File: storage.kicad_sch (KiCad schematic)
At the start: 14 parts, among them J11 microSD, Molex 104031-0811 pu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, U24 W25Q128JVSIQ, 128 Mbit QSPI N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

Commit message: Replace BMI088 with ICM-45686; vendor all footprints and 3D models for layout
Sensors: U21 is now the TDK ICM-45686 (single AP_CS on GPIO20 as IMU_CS,
INT1/INT2 on GPIO23/24, GPIO21 spare, R49 dropped, VDD+VDDIO on V3V3_ANA
with 100 nF + 1 uF each). Project-local symbol, footprint and stand-in STEP;
footprint numbering verified against DS-000577 Rev 1.0 Sec 11.2 (CCW, top
view). BMI088_SPI derived-symbol machinery removed from the generator.

Layout readiness: new tools/audit_footprints.py checks every component for
a resolvable footprint and present 3D model (128/128 OK). The seven official
KiCad footprints whose STEP files are absent from kicad-packages3d 10.0.6
are vendored into MARV_Packages.pretty with project-local models in
MARV_Packages.3dshapes: manufacturer STEPs (Coilcraft XGL4030, Molex
104031-0811), EasyEDA model (HRO TYPE-C-31-M-12), FreeCAD-generated bodies
from tools/3d/ (RP2354B QFN-80, TPS62913 RPU0010A, TPS2121 RUX0012A, Amass
XT30PW-M), and KiCad generic stand-ins (BMP581, ADXL375). Model offsets were
derived by measurement and confirmed in a rendered check board.
PROVENANCE.md records source, licence and SHA256 per model; LIBRARIES.md
lists the pre-fab 3D-viewer checks and the unverified dimensions.

Checks: build idempotent, ERC 0/0, check_power_netlist 149 mappings /
128 components, run_power_checks PASS, audit 0 needing action.

Co-Authored-By: Claude Fable 5.1 <noreply@anthropic.com>
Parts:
- J11: footprint Connector_Card:microSD_HC_Molex_104031-0811 -> MARV_Packages:microSD_HC_Molex_104031-0811

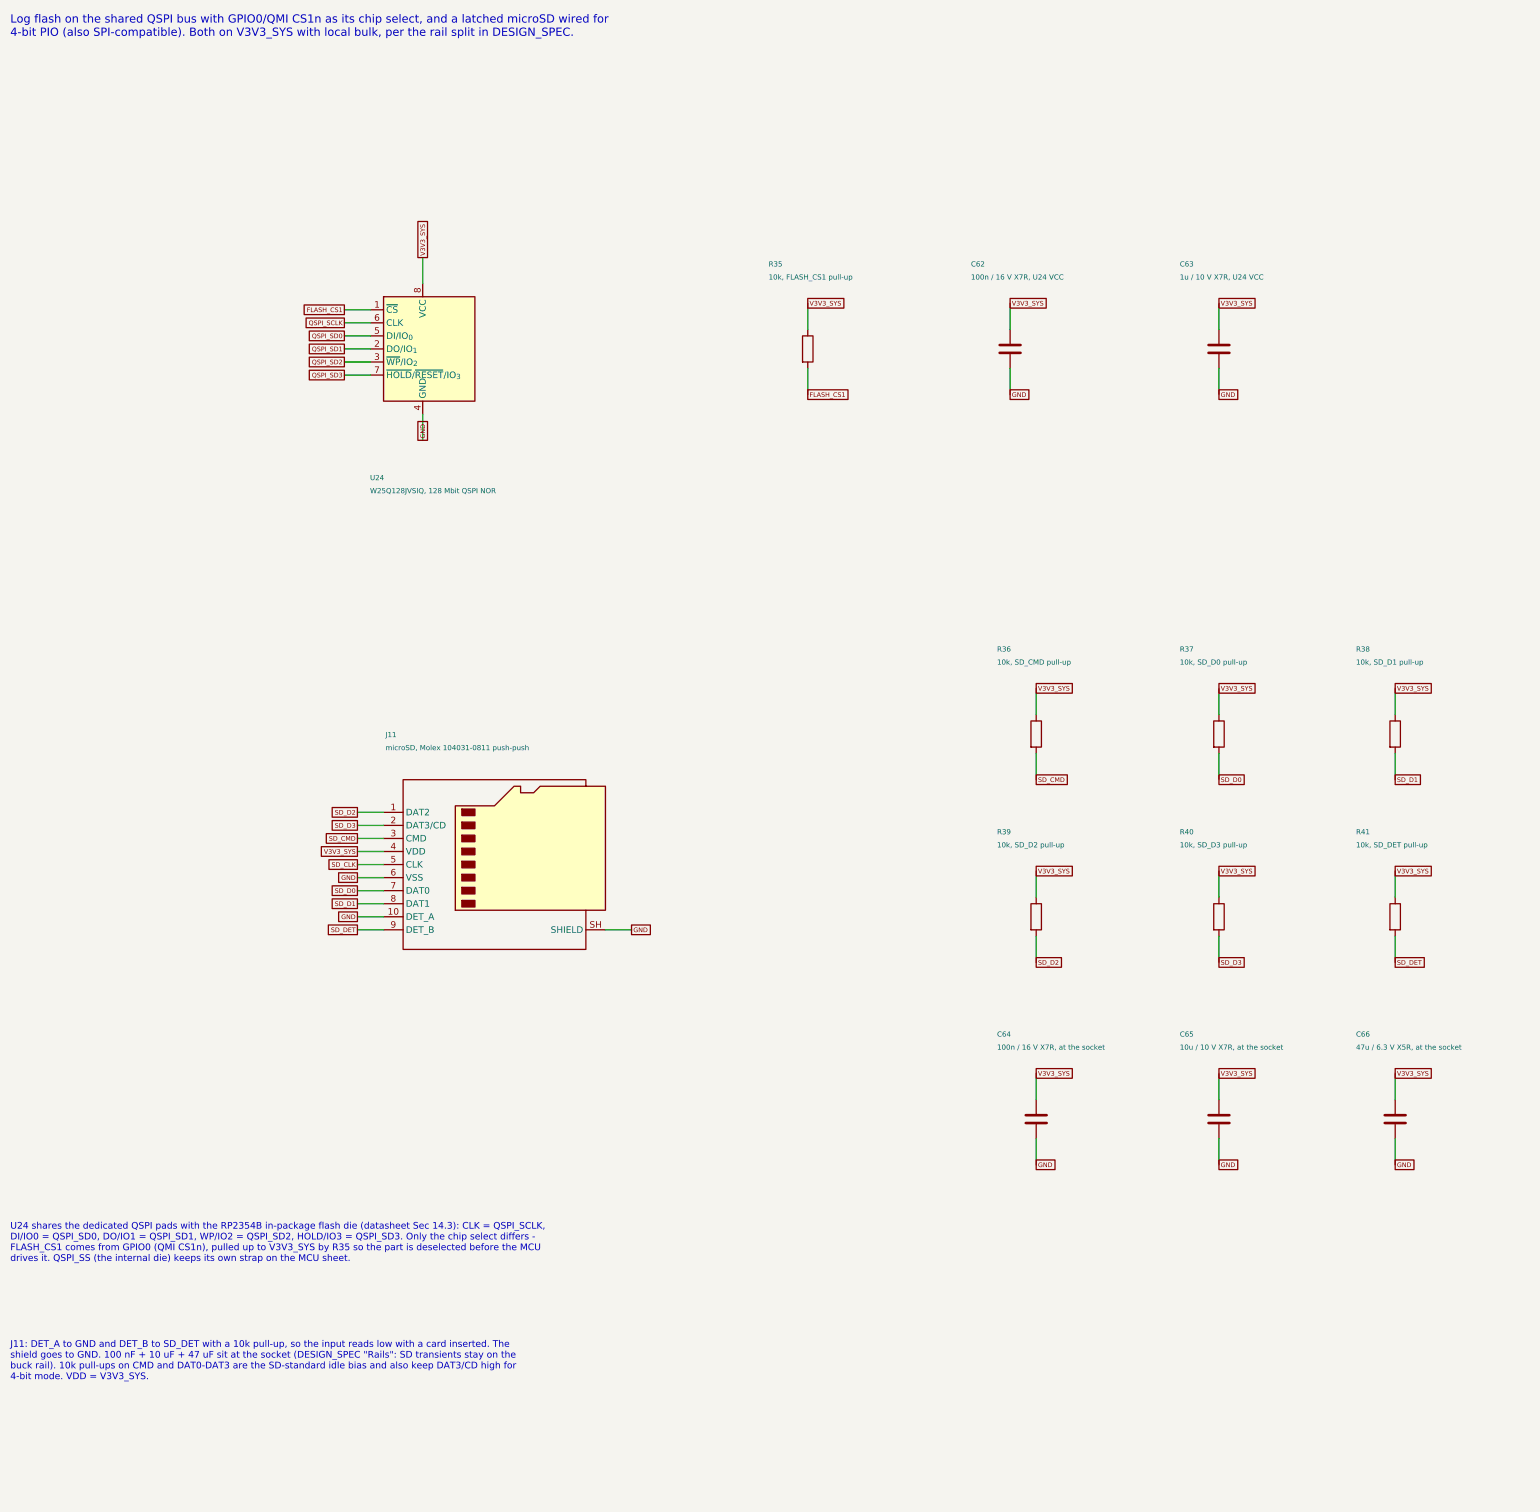
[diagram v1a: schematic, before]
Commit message: Physical design: VBAT-in buck, ESC pad row, pad-row IO, 50 mm single-sided board
Power: the FC now takes raw 2-6S VBAT from the MicoAir AM32 4-in-1 ESC pad
row (CURR TX M4 M3 M2 M1 VBAT GND, J3) through an AP63205WU 5 V/2 A buck
(U26, XGL4030-472, 3 x 22 uF) into the existing TPS2121 mux; XT30 and its
TVS removed. VBAT sense 100k/10k (36 V FS) on ADC0, ESC current sense on
ADC2, ESC KISS telemetry on GPIO30.

IO per the physical spec (DESIGN_SPEC "Physical design"): solder pad rows
for GPS/ELRS/MAG (JST-GH removed), DBG and buzzer; 3x4 servo block for
PWM5-8; 2x6 spare-IO block; WS2812C-2020 RGB LED replaces the two discrete
LEDs; buzzer moved off-board to pads; flash socket is the 150-mil SOIC-8
(W25Q64 default, APS6404L PSRAM alternative); four 4.0 mm grommet holes on
the 30.5 mm pattern. Passives moved to 0402/0603 for the single-sided
envelope.

Board: tools/setup_pcb.py regenerates MARV-V2.kicad_pcb from the netlist —
50 x 50 mm, 4-layer JLC 7628 stack-up, net classes incl. a 90 ohm USB pair,
edge-anchored connectors, coarse interior placement, silk pad labels.
DRC leaves only unrouted items. The BMP581 project footprint had its 2-pad
edges at +/-0.5 mm (corner pads overlapped, three nets shorted); corrected
to Bosch Fig. 32 (+/-0.25 mm, 0.20 mm gaps).

Checks: ERC 0/0, 217 pin mappings / 139 components, run_power_checks PASS,
audit 139/139, pcb DRC unrouted-only.

Co-Authored-By: Claude Fable 5.1 <noreply@anthropic.com>
Claude-Session: https://claude.ai/code/session_01U6Ud7JA3CDTJZVcZZr5sx1
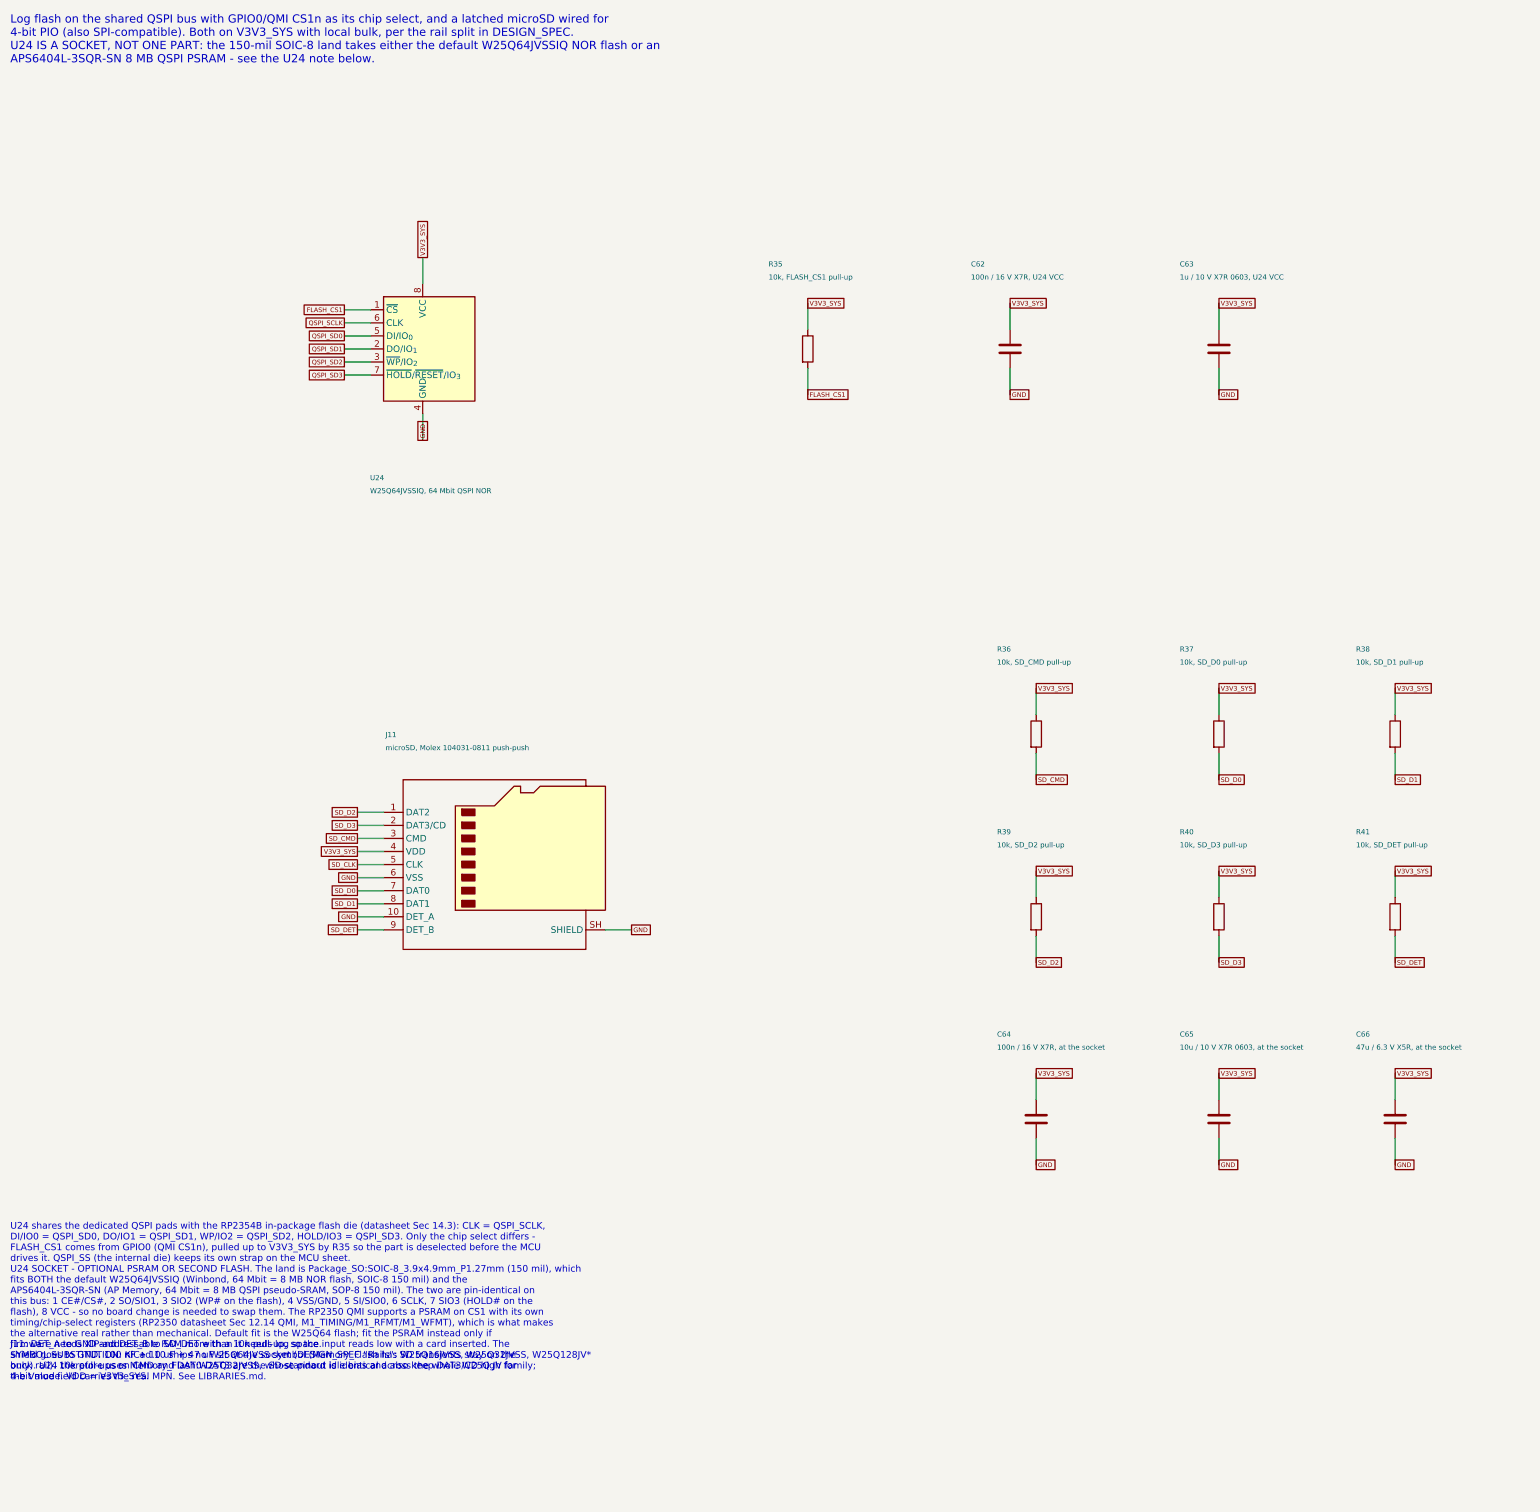
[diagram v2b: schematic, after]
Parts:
- C62, C64: footprint Capacitor_SMD:C_0805_2012Metric -> Capacitor_SMD:C_0402_1005Metric
- C63: value 1u / 10 V X7R, U24 VCC -> 1u / 10 V X7R 0603, U24 VCC; footprint Capacitor_SMD:C_0805_2012Metric -> Capacitor_SMD:C_0603_1608Metric
- C65: value 10u / 10 V X7R, at the socket -> 10u / 10 V X7R 0603, at the socket; footprint Capacitor_SMD:C_1206_3216Metric -> Capacitor_SMD:C_0603_1608Metric
- R35, R36, R37, R38, R39, R40, R41: footprint Resistor_SMD:R_0603_1608Metric -> Resistor_SMD:R_0402_1005Metric
- U24: value W25Q128JVSIQ, 128 Mbit QSPI NOR -> W25Q64JVSSIQ, 64 Mbit QSPI NOR; footprint Package_SO:SOIC-8_5.3x5.3mm_P1.27mm -> Package_SO:SOIC-8_3.9x4.9mm_P1.27mm; symbol Memory_Flash:W25Q128JVS -> Memory_Flash:W25Q32JVSS
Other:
- note added: "Log flash on the shared QSPI bus with GPIO0/QMI CS1n as its chip select, and a latched microSD wired for 4-bit PIO (also SPI-compatible). Both on V3V3_SYS with local bulk, per the rail split in DESIGN_SPEC. U24 IS A SOCKET, NOT ONE PART: the 150-mil SOIC-8 land takes either the default W25Q64JVSSIQ NOR flash or an APS6404L-3SQR-SN 8 MB QSPI PSRAM - see the U24 note below."
- note removed: "Log flash on the shared QSPI bus with GPIO0/QMI CS1n as its chip select, and a latched microSD wired for 4-bit PIO (also SPI-compatible). Both on V3V3_SYS with local bulk, per the rail split in DESIGN_SPEC."

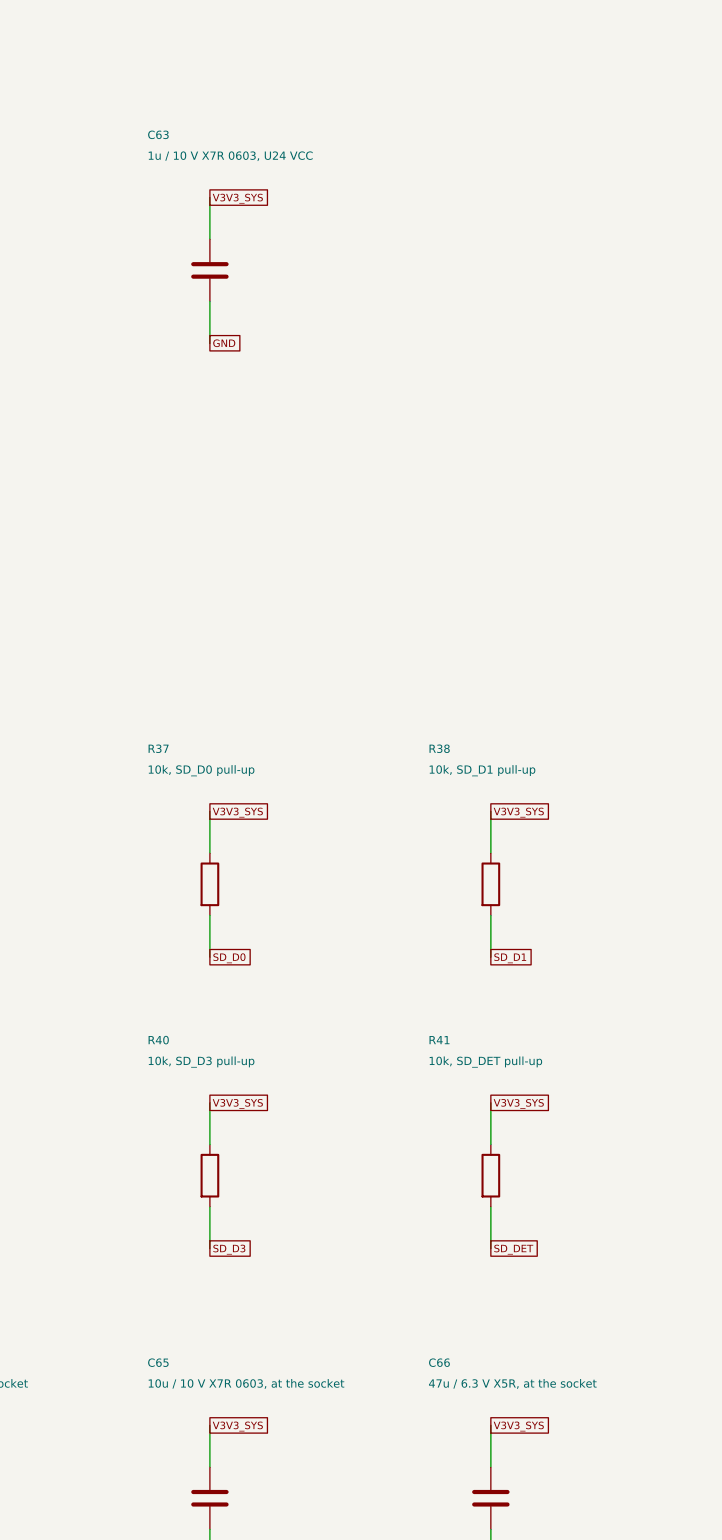
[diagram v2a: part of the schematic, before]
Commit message: Remove buzzer; passives to 0201/0402; GPIO28 to spare-IO block
Buzzer pads J15, driver Q20/D22/R33/R34 and the BUZZ nets removed; GPIO28
now terminates on J16 pin 12 (was a second GND). Resistors 0201, caps
<= 4.7 uF 0402, 22 uF/10 V 0603, 22 uF/25 V and 10 uF/50 V 0805, 47 uF
0805; USB net-class clearance 0.18 mm so the 0201 series resistors on the
pair pass DRC. Board regenerated at 50 x 50 mm (courtyard fill 63.5 %);
DRC unrouted-only. 134 components, 105 nets; ERC 0/0, 213 pin mappings,
run_power_checks PASS, audit 134/134.

Co-Authored-By: Claude Fable 5.1 <noreply@anthropic.com>
Claude-Session: https://claude.ai/code/session_01U6Ud7JA3CDTJZVcZZr5sx1
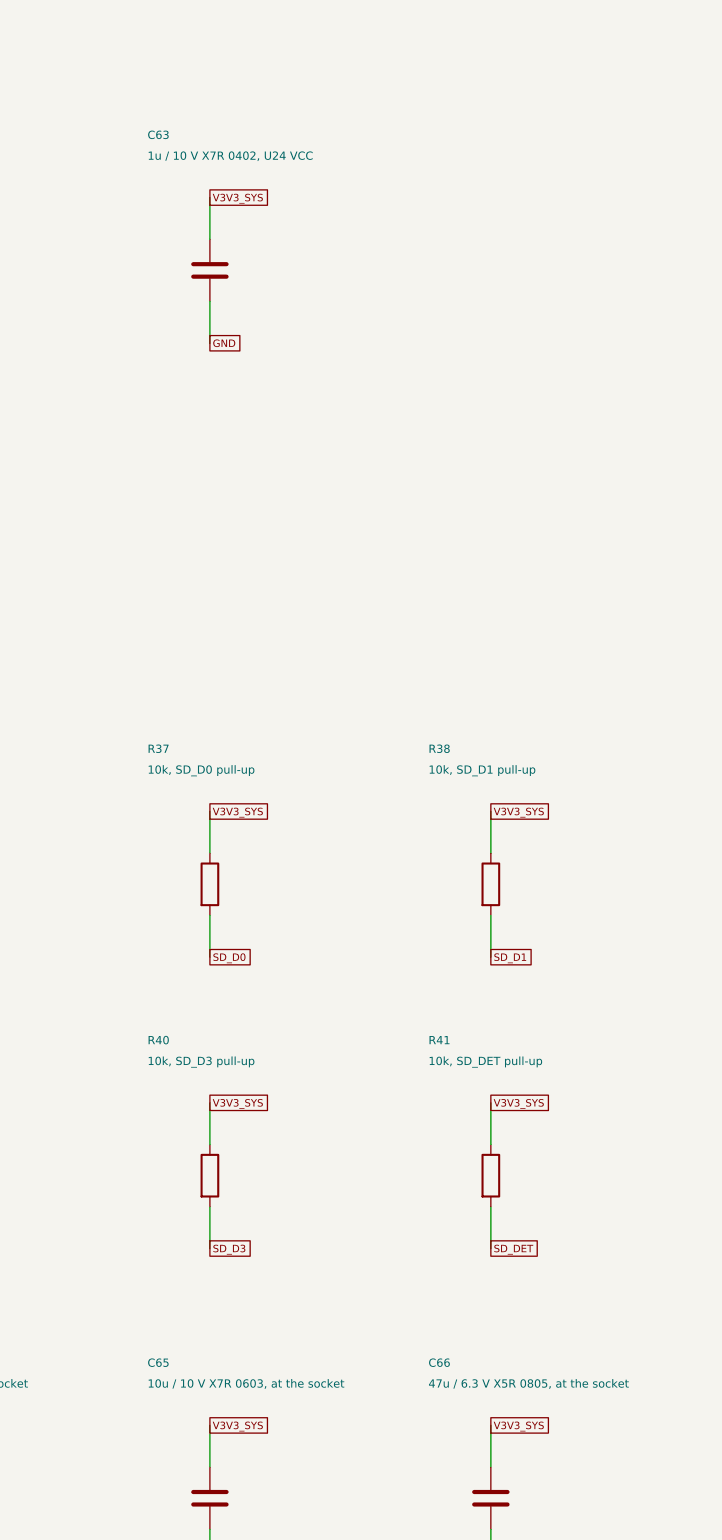
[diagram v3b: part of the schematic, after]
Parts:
- C63: value 1u / 10 V X7R 0603, U24 VCC -> 1u / 10 V X7R 0402, U24 VCC; footprint Capacitor_SMD:C_0603_1608Metric -> Capacitor_SMD:C_0402_1005Metric
- C66: value 47u / 6.3 V X5R, at the socket -> 47u / 6.3 V X5R 0805, at the socket; footprint Capacitor_SMD:C_1210_3225Metric -> Capacitor_SMD:C_0805_2012Metric
- R35, R36, R37, R38, R39, R40, R41: footprint Resistor_SMD:R_0402_1005Metric -> Resistor_SMD:R_0201_0603Metric
